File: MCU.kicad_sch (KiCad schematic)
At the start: 12 parts, among them J1 SWD, SW1 SW_Push, U1 STM32G431KBUx, Y1 8MHz_SMD3225

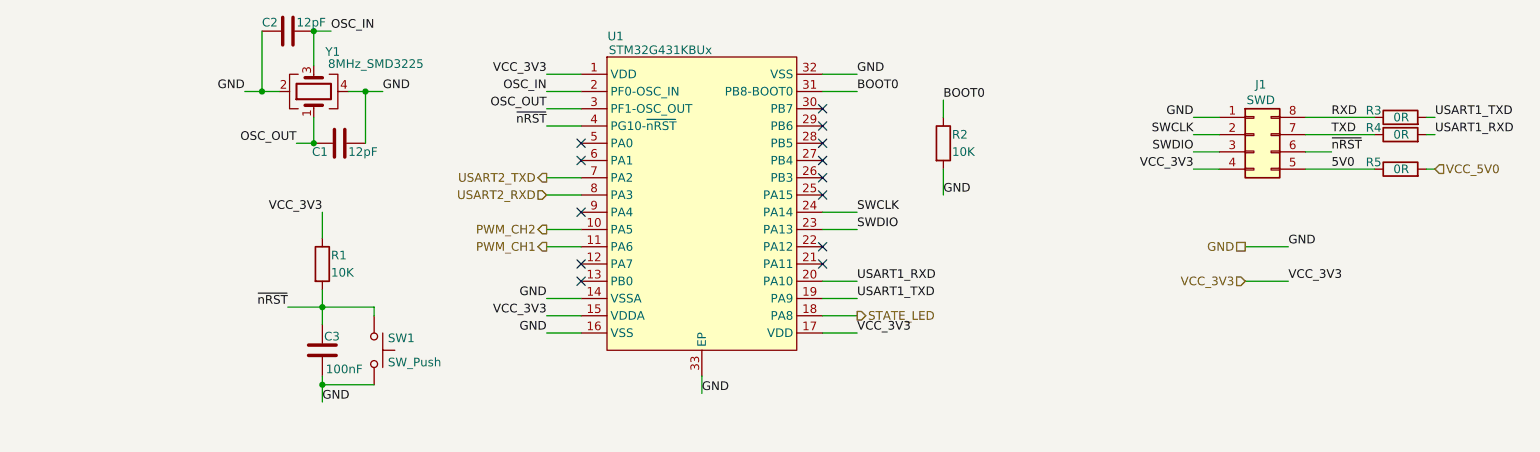
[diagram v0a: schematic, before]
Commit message: [New]: 完成整个原理图绘制和ERC检查
JIRA-ID: N/A

完成整个原理图绘制和ERC检查
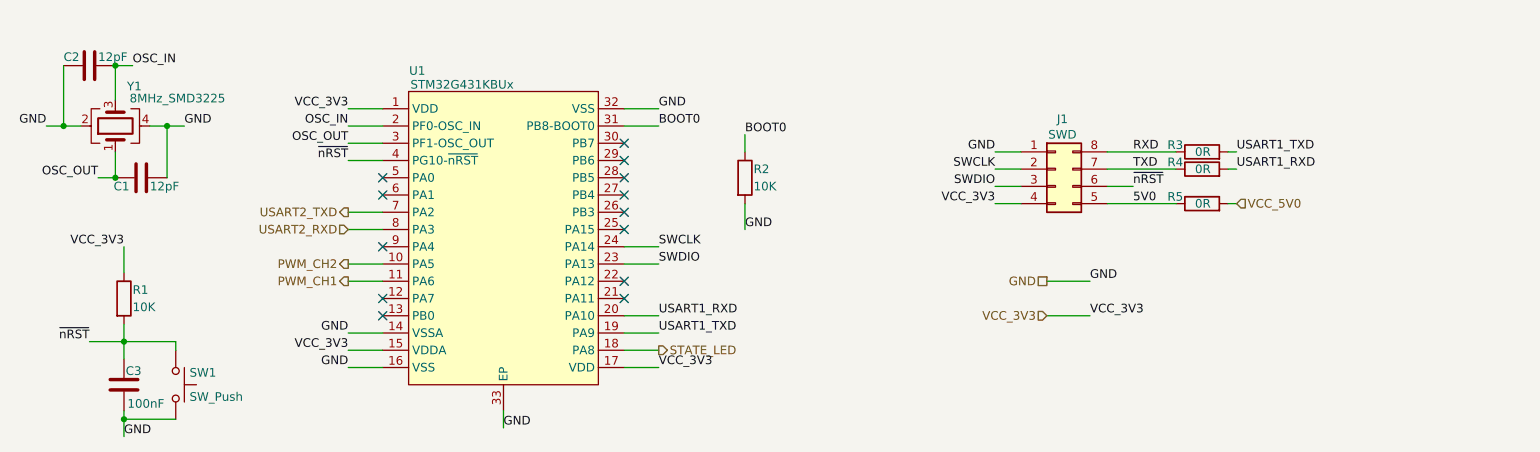
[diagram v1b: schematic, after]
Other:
- moved on the sheet: C1, C2, C3, J1, R1, R2, R3, R4, R5, SW1, U1, Y1

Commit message: [Fix]: 添加雷达供电隔离
JIRA-ID: N/A

添加雷达信号隔离电路，检查原理图错误，新增原理图符号
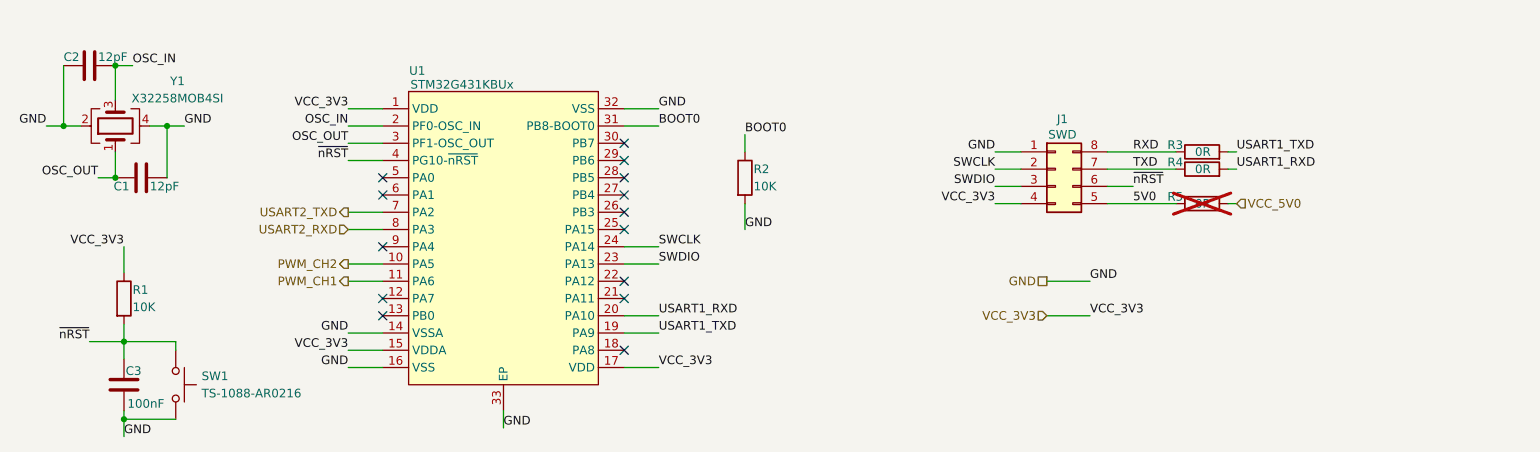
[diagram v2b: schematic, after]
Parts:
- removed SW1: SW_Push, symbol Switch:SW_Push
- removed Y1: 8MHz_SMD3225, symbol Device:Crystal_GND24
- added SW1: TS-1088-AR0216, symbol lidar_camera_sync:TS-1088-AR0216
- added Y1: X32258MOB4SI, symbol lidar_camera_sync:X32258MOB4SI
- R5: now not fitted
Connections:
- net GND: now also SW1.2, Y1.2, Y1.4
- net OSC_IN: now also Y1.3
- net OSC_OUT: now also Y1.1
- net ~{nRST}: now also SW1.1
- net STATE_LED: no longer names the net of U1.18 (PA8)
- no-connect marks 13 -> 14
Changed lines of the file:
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@@
+	)
+	(no_connect
+		(at 144.78 120.65)
 	)
 	(no_connect
@@
 		(pts
 			(xy 215.9 91.44) (xy 226.06 91.44)
-		)
-		(stroke
-			(width 0)
-			(type default)
-		)
-	)
-	(wire
-		(pts
-			(xy 144.78 120.65) (xy 149.86 120.65)
 		)
 		(stroke
@@
 			)
 			(justify right)
-		)
-	)
-	(hierarchical_label "STATE_LED"
-		(shape output)
-		(at 149.86 120.65 0)
-		(effects
-			(font
-				(size 1.27 1.27)
-			)
-			(justify left)
 		)
 	)
@@
 		(in_bom yes)
 		(on_board yes)
-		(dnp no)
+		(dnp yes)
 		(property "Reference" "R5"
 			(at 227.076 98.044 90)
@@
 	)
 	(symbol
+		(lib_id "lidar_camera_sync:X32258MOB4SI")
+		(at 69.85 87.63 90)
+		(unit 1)
+		(exclude_from_sim no)
+		(in_bom yes)
+		(on_board yes)
+		(dnp no)
+		(property "Reference" "Y1"
+			(at 78.994 81.026 90)
+			(effects
+				(font
+					(size 1.27 1.27)
+				)
+			)
+		)
+		(property "Value" "X32258MOB4SI"
+			(at 78.994 83.566 90)
+			(effects
+				(font
+					(size 1.27 1.27)
+				)
+			)
+		)
+		(property "Footprint" ""
+			(at 69.85 87.63 0)
+			(effects
+				(font
+					(size 1.27 1.27)
+				)
+				(hide yes)
+			)
+		)
+		(property "Datasheet" "~"
+			(at 69.85 87.63 0)
+			(effects
+				(font
+					(size 1.27 1.27)
+				)
+				(hide yes)
+			)
+		)
+		(property "Description" "Four pin crystal, GND on pins 2 and 4, 12pF"
+			(at 69.85 87.63 0)
+			(effects
+				(font
+					(size 1.27 1.27)
+				)
+				(hide yes)
+			)
+		)
+		(pin "4"
+		)
+		(pin "1"
+		)
+		(pin "3"
+		)
+		(pin "2"
+		)
+		(instances
+			(project ""
+				(path "/4d41fa76-12ab-4867-bf30-96d46704f2ab/66dd57c5-fcd2-4ccb-bf38-17b55711c2d9"
+					(reference "Y1")
+					(unit 1)
+				)
+			)
+		)
+	)
+	(symbol
 		(lib_id "Device:C")
 		(at 73.66 95.25 270)
@@
 	)
 	(symbol
-		(lib_id "Device:Crystal_GND24")
-		(at 69.85 87.63 90)
-		(unit 1)
-		(exclude_from_sim no)
-		(in_bom yes)
-		(on_board yes)
-		(dnp no)
-		(property "Reference" "Y1"
-			(at 72.644 81.788 90)
-			(effects
-				(font
-					(size 1.27 1.27)
-				)
-			)
-		)
-		(property "Value" "8MHz_SMD3225"
-			(at 78.994 83.566 90)
-			(effects
-				(font
-					(size 1.27 1.27)
-				)
-			)
-		)
-		(property "Footprint" ""
-			(at 69.85 87.63 0)
-			(effects
-				(font
-					(size 1.27 1.27)
-				)
-				(hide yes)
-			)
-		)
-		(property "Datasheet" "~"
-			(at 69.85 87.63 0)
-			(effects
-				(font
-					(size 1.27 1.27)
-				)
-				(hide yes)
-			)
-		)
-		(property "Description" "Four pin crystal, GND on pins 2 and 4"
-			(at 69.85 87.63 0)
-			(effects
-				(font
-					(size 1.27 1.27)
-				)
-				(hide yes)
-			)
-		)
-		(pin "1"
-		)
-		(pin "3"
-		)
-		(pin "2"
-		)
-		(pin "4"
-		)
-		(instances
-			(project ""
-				(path "/4d41fa76-12ab-4867-bf30-96d46704f2ab/66dd57c5-fcd2-4ccb-bf38-17b55711c2d9"
-					(reference "Y1")
-					(unit 1)
-				)
-			)
-		)
-	)
-	(symbol
-		(lib_id "Switch:SW_Push")
+		(lib_id "lidar_camera_sync:TS-1088-AR0216")
 		(at 78.74 125.73 270)
 		(unit 1)
@@
 		(on_board yes)
 		(dnp no)
+		(fields_autoplaced yes)
 		(property "Reference" "SW1"
-			(at 80.772 123.952 90)
+			(at 82.55 124.4599 90)
 			(effects
 				(font
@@
 			)
 		)
-		(property "Value" "SW_Push"
-			(at 80.772 127.508 90)
+		(property "Value" "TS-1088-AR0216"
+			(at 82.55 126.9999 90)
 			(effects
 				(font
@@
 			)
 		)
+		(pin "1"
+		)
 		(pin "2"
 		)
-		(pin "1"
-		)
 		(instances

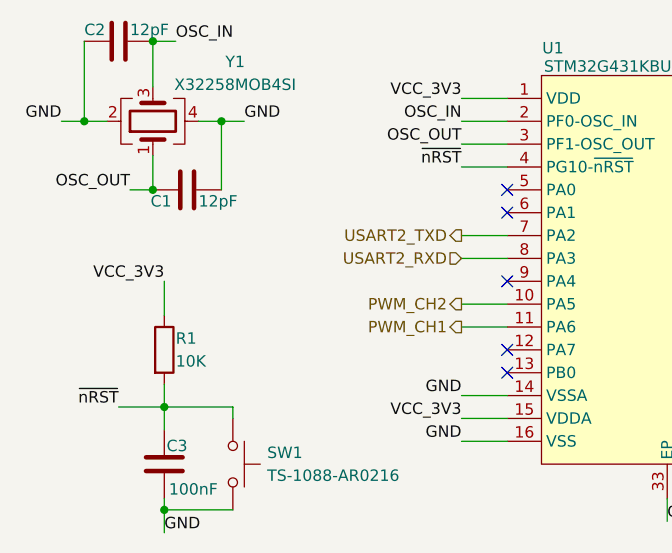
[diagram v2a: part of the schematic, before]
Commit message: [Modify]: 完成封装的分配和PCB更新
JIRA-ID: N/A

完成封装的分配和从原理图到PCB的初始更新;完成DRC检查
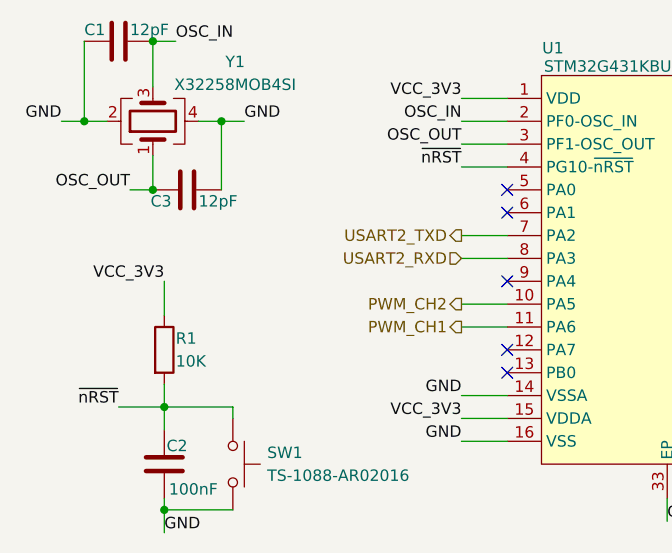
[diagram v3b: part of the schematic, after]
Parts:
- removed SW1: TS-1088-AR0216, symbol lidar_camera_sync:TS-1088-AR0216
- added SW1: TS-1088-AR02016, lidar_camera_sync:TS-1088-AR02016, symbol lidar_camera_sync:TS-1088-AR02016
- C1: renamed from C2; footprint (none) -> Capacitor_SMD:C_0603_1608Metric
- C2: renamed from C3; footprint (none) -> Capacitor_SMD:C_0603_1608Metric
- C3: renamed from C1; footprint (none) -> Capacitor_SMD:C_0603_1608Metric
- J1: footprint (none) -> Connector_PinHeader_2.54mm:PinHeader_2x04_P2.54mm_Vertical
- R1, R2, R3, R4, R5: footprint (none) -> Resistor_SMD:R_0603_1608Metric
- U1: footprint (none) -> lidar_camera_sync:UFQFPN32-5.3x5.3_P0.5
- Y1: footprint (none) -> lidar_camera_sync:SMD3225
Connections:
- net GND: now also SW1.2
- net ~{nRST}: now also SW1.1
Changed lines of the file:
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@@
 			)
 		)
-		(property "Footprint" ""
+		(property "Footprint" "Resistor_SMD:R_0603_1608Metric"
 			(at 160.782 95.25 90)
 			(effects
@@
 		(on_board yes)
 		(dnp no)
-		(property "Reference" "C3"
+		(property "Reference" "C2"
 			(at 71.374 123.698 0)
 			(effects
@@
 			)
 		)
-		(property "Footprint" ""
+		(property "Footprint" "Capacitor_SMD:C_0603_1608Metric"
 			(at 72.0852 129.54 0)
 			(effects
@@
 			(project "lidar_camera_sync"
 				(path "/4d41fa76-12ab-4867-bf30-96d46704f2ab/66dd57c5-fcd2-4ccb-bf38-17b55711c2d9"
-					(reference "C3")
+					(reference "C2")
 					(unit 1)
 				)
@@
 			)
 		)
-		(property "Footprint" ""
+		(property "Footprint" "Resistor_SMD:R_0603_1608Metric"
 			(at 229.87 100.838 90)
 			(effects
@@
 			)
 		)
-		(property "Footprint" ""
+		(property "Footprint" "lidar_camera_sync:UFQFPN32-5.3x5.3_P0.5"
 			(at 127 104.14 0)
 			(effects
@@
 			)
 		)
-		(property "Footprint" ""
+		(property "Footprint" "lidar_camera_sync:SMD3225"
 			(at 69.85 87.63 0)
 			(effects
@@
 		(on_board yes)
 		(dnp no)
-		(property "Reference" "C1"
+		(property "Reference" "C3"
 			(at 69.596 96.52 90)
 			(effects
@@
 			)
 		)
-		(property "Footprint" ""
+		(property "Footprint" "Capacitor_SMD:C_0603_1608Metric"
 			(at 69.85 96.2152 0)
 			(effects
@@
 			(project ""
 				(path "/4d41fa76-12ab-4867-bf30-96d46704f2ab/66dd57c5-fcd2-4ccb-bf38-17b55711c2d9"
-					(reference "C1")
+					(reference "C3")
 					(unit 1)
 				)
@@
 			)
 		)
-		(property "Footprint" ""
+		(property "Footprint" "Connector_PinHeader_2.54mm:PinHeader_2x04_P2.54mm_Vertical"
 			(at 208.28 93.98 0)
 			(effects
@@
 			)
 		)
-		(property "Footprint" ""
+		(property "Footprint" "Resistor_SMD:R_0603_1608Metric"
 			(at 229.87 95.758 90)
 			(effects
@@
 	)
 	(symbol
-		(lib_id "lidar_camera_sync:TS-1088-AR0216")
+		(lib_id "Device:C")
+		(at 66.04 78.74 270)
+		(unit 1)
+		(exclude_from_sim no)
+		(in_bom yes)
+		(on_board yes)
+		(dnp no)
+		(property "Reference" "C1"
+			(at 62.23 77.47 90)
+			(effects
+				(font
+					(size 1.27 1.27)
+				)
+				(justify left)
+			)
+		)
+		(property "Value" "12pF"
+			(at 67.31 77.47 90)
+			(effects
+				(font
+					(size 1.27 1.27)
+				)
+				(justify left)
+			)
+		)
+		(property "Footprint" "Capacitor_SMD:C_0603_1608Metric"
+			(at 62.23 79.7052 0)
+			(effects
+				(font
+					(size 1.27 1.27)
+				)
+				(hide yes)
+			)
+		)
+		(property "Datasheet" "~"
+			(at 66.04 78.74 0)
+			(effects
+				(font
+					(size 1.27 1.27)
+				)
+				(hide yes)
+			)
+		)
+		(property "Description" "Unpolarized capacitor"
+			(at 66.04 78.74 0)
+			(effects
+				(font
+					(size 1.27 1.27)
+				)
+				(hide yes)
+			)
+		)
+		(pin "1"
+		)
+		(pin "2"
+		)
+		(instances
+			(project "lidar_camera_sync"
+				(path "/4d41fa76-12ab-4867-bf30-96d46704f2ab/66dd57c5-fcd2-4ccb-bf38-17b55711c2d9"
+					(reference "C1")
+					(unit 1)
+				)
+			)
+		)
+	)
+	(symbol
+		(lib_id "lidar_camera_sync:TS-1088-AR02016")
 		(at 78.74 125.73 270)
 		(unit 1)
@@
 			)
 		)
-		(property "Value" "TS-1088-AR0216"
+		(property "Value" "TS-1088-AR02016"
 			(at 82.55 126.9999 90)
 			(effects
@@
 			)
 		)
-		(property "Footprint" ""
+		(property "Footprint" "lidar_camera_sync:TS-1088-AR02016"
 			(at 83.82 125.73 0)
 			(effects
@@
 			)
 		)
-		(pin "1"
-		)
-		(pin "2"
+		(pin "2"
+		)
+		(pin "1"
 		)
 		(instances
@@
 				(path "/4d41fa76-12ab-4867-bf30-96d46704f2ab/66dd57c5-fcd2-4ccb-bf38-17b55711c2d9"
 					(reference "SW1")
-					(unit 1)
-				)
-			)
-		)
-	)
-	(symbol
-		(lib_id "Device:C")
-		(at 66.04 78.74 270)
-		(unit 1)
-		(exclude_from_sim no)
-		(in_bom yes)
-		(on_board yes)
-		(dnp no)
-		(property "Reference" "C2"
-			(at 62.23 77.47 90)
-			(effects
-				(font
-					(size 1.27 1.27)
-				)
-				(justify left)
-			)
-		)
-		(property "Value" "12pF"
-			(at 67.31 77.47 90)
-			(effects
-				(font
-					(size 1.27 1.27)
-				)
-				(justify left)
-			)
-		)
-		(property "Footprint" ""
-			(at 62.23 79.7052 0)
-			(effects
-				(font
-					(size 1.27 1.27)
-				)
-				(hide yes)
-			)
-		)
-		(property "Datasheet" "~"
-			(at 66.04 78.74 0)
-			(effects
-				(font
-					(size 1.27 1.27)
-				)
-				(hide yes)
-			)
-		)
-		(property "Description" "Unpolarized capacitor"
-			(at 66.04 78.74 0)
-			(effects
-				(font
-					(size 1.27 1.27)
-				)
-				(hide yes)
-			)
-		)
-		(pin "1"
-		)
-		(pin "2"
-		)
-		(instances
-			(project "lidar_camera_sync"
-				(path "/4d41fa76-12ab-4867-bf30-96d46704f2ab/66dd57c5-fcd2-4ccb-bf38-17b55711c2d9"
-					(reference "C2")
 					(unit 1)
 				)
@@
 			)
 		)
-		(property "Footprint" ""
+		(property "Footprint" "Resistor_SMD:R_0603_1608Metric"
 			(at 229.87 93.218 90)
 			(effects
@@
 			)
 		)
-		(property "Footprint" ""
+		(property "Footprint" "Resistor_SMD:R_0603_1608Metric"
 			(at 69.342 113.03 90)
 			(effects

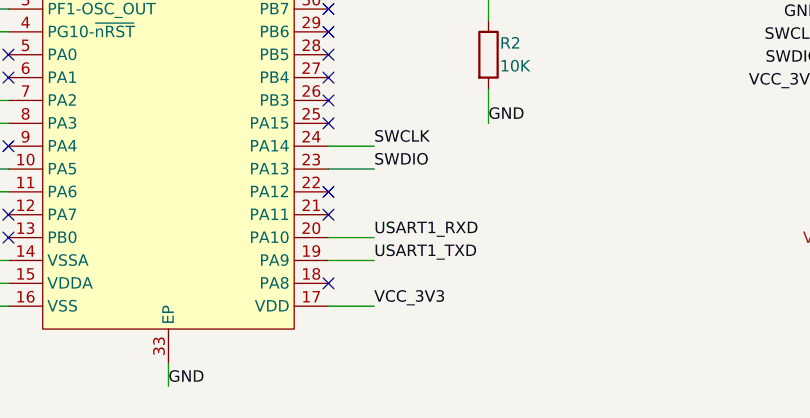
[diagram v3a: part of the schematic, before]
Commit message: [Modify]: 添加输入输出去耦电容以及WS2812B灯珠
JIRA-ID: N/A

添加输入输出去耦电容以及WS2812B灯珠
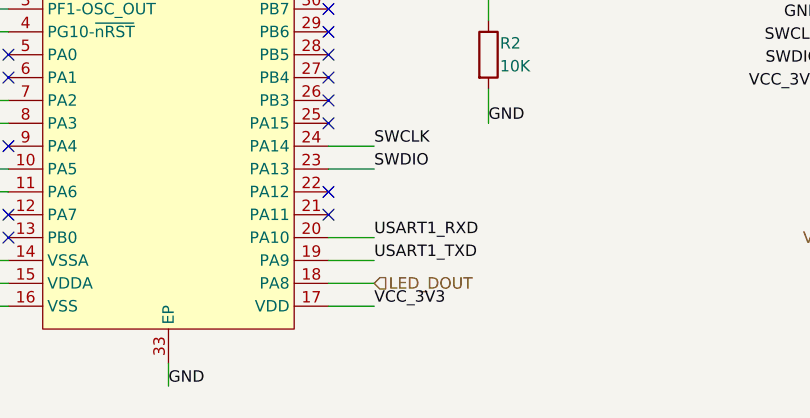
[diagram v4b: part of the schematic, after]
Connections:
- net LED_DOUT: now reaches U1.18 (PA8)
- no-connect marks 14 -> 13
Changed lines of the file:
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@@
-	)
-	(no_connect
-		(at 144.78 120.65)
 	)
 	(no_connect
@@
 		(pts
 			(xy 104.14 90.17) (xy 109.22 90.17)
+		)
+		(stroke
+			(width 0)
+			(type default)
+		)
+	)
+	(wire
+		(pts
+			(xy 144.78 120.65) (xy 149.86 120.65)
 		)
 		(stroke
@@
 		)
 	)
+	(hierarchical_label "LED_DOUT"
+		(shape input)
+		(at 149.86 120.65 0)
+		(effects
+			(font
+				(size 1.27 1.27)
+			)
+			(justify left)
+		)
+	)

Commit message: [Modify]: 修复一些封装错误, 完成基本Layout器件摆放
JIRA-ID: N/A

修复一些封装错误, 完成基本Layout器件摆放
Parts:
- J1: footprint Connector_PinHeader_2.54mm:PinHeader_2x04_P2.54mm_Vertical -> lidar_camera_sync:Pinheader_2x04_P2.54mm
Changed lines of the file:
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@@
 			)
 		)
-		(property "Footprint" "Connector_PinHeader_2.54mm:PinHeader_2x04_P2.54mm_Vertical"
+		(property "Footprint" "lidar_camera_sync:Pinheader_2x04_P2.54mm"
 			(at 208.28 93.98 0)
 			(effects
